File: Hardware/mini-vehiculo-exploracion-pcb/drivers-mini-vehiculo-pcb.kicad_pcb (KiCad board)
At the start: 2 copper layers, 7 parts, among them IC1 MAX8891EXK33_V+T, U1 TPS561208DDCR, U3 DRV8873HPWPRQ1, U4 DRV8873HPWPRQ1

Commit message: updated driver pcb
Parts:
- added C1: 0.1u, capacitores_driver:CAPC2012X88N, F.Cu at (75.1, 114.4)
- added C11: 1u, capacitores_driver:CAPC2012X88N, F.Cu at (61.0, 128.0)
- added C12: 0.1u, capacitores_driver:CAPC2012X88N, F.Cu at (75.1, 129.5)
- added C13: 47n, capacitores_driver:CAPC2012X140N, F.Cu at (61.6, 123.0)
- added C2: 0.1u, capacitores_driver:CAPC2012X88N, F.Cu at (75.1, 117.4)
- added C3: 1u, capacitores_driver:CAPC2012X88N, F.Cu at (75.1, 120.5)
- added C4: 1u, capacitores_driver:CAPC2012X88N, F.Cu at (75.1, 123.5)
- added C6: 1u, capacitores_driver:CAPC2012X88N, F.Cu at (66.6, 109.5)
- added C7: 0.1u, capacitores_driver:CAPC2012X88N, F.Cu at (75.1, 126.5)
- added C8: 47n, capacitores_driver:CAPC2012X140N, F.Cu at (58.6, 105.5)

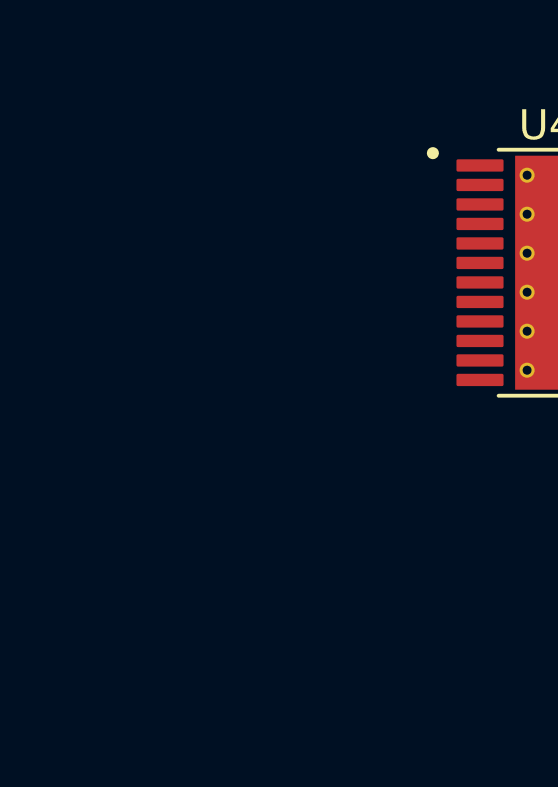
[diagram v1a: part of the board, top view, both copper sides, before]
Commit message: updated resistor footprint
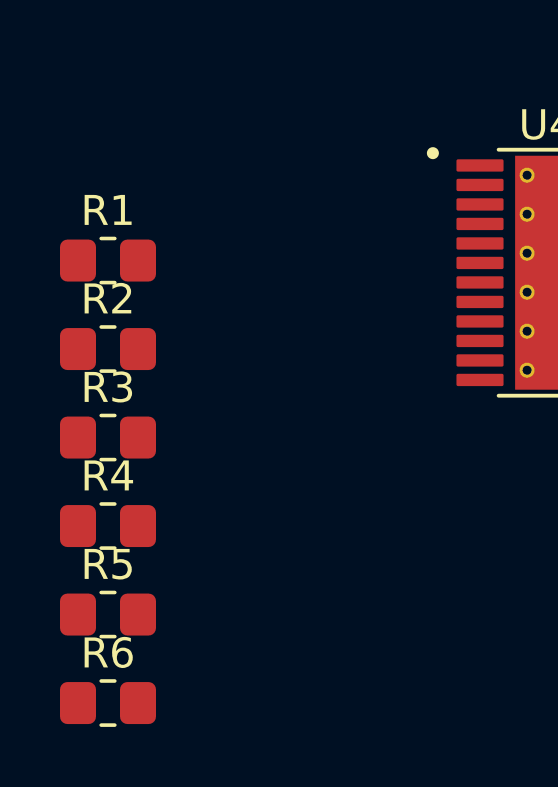
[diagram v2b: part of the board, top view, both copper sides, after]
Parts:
- added R1: 820, Resistor_SMD:R_0805_2012Metric_Pad1.20x1.40mm_HandSolder, F.Cu at (33.0, 124.2)
- added R2: 820, Resistor_SMD:R_0805_2012Metric_Pad1.20x1.40mm_HandSolder, F.Cu at (33.0, 127.2)
- added R3: 820, Resistor_SMD:R_0805_2012Metric_Pad1.20x1.40mm_HandSolder, F.Cu at (33.0, 130.2)
- added R4: 820, Resistor_SMD:R_0805_2012Metric_Pad1.20x1.40mm_HandSolder, F.Cu at (33.0, 133.1)
- added R5: 10k, Resistor_SMD:R_0805_2012Metric_Pad1.20x1.40mm_HandSolder, F.Cu at (33.0, 136.1)
- added R6: 10k, Resistor_SMD:R_0805_2012Metric_Pad1.20x1.40mm_HandSolder, F.Cu at (33.0, 139.0)

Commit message: updated pcb drv
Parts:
- added C1: 180u, EMZR160ARA221MF61G:CAPAE660X610N, F.Cu at (38.4, 61.5)
- added C7: 180u, EMZR160ARA221MF61G:CAPAE660X610N, F.Cu at (38.4, 109.5)
- added J1: Conn_01x08_Pin_drv, JST_Connectors:JST_8PIN, F.Cu at (54.0, 44.5)
- F1: value SMD200F_24-2920-2 -> SF-1206SA1500R-2; footprint SMD200F_24-2920:SMD200F2429202 -> SF-1206SA1500R-2:SF1206SA1500R2
- moved R2 64.4 mm to (39.5, 72.0)
- moved C4 50.0 mm to (72.6, 76.5)
- moved R1 48.7 mm to (35.0, 78.5)
- moved R5 47.1 mm to (40.5, 92.5)
- moved R3 46.9 mm to (41.0, 78.0)
- moved C2 42.3 mm to (66.6, 73.0)
- moved C11 39.1 mm to (112.5, 112.0)
- moved C5 39.1 mm to (112.5, 109.0)
- moved C10 35.8 mm to (67.4, 94.5)
- moved R6 34.8 mm to (37.0, 98.5)
- moved R4 34.5 mm to (42.5, 97.0)
- moved C12 29.4 mm to (62.0, 93.6), turned to 90 degrees
- moved C3 28.7 mm to (68.2, 80.8)
- moved C6 28.7 mm to (60.2, 76.8)
- moved C9 28.7 mm to (62.5, 99.3)
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- renumbered C12 to C10, C4 to C11, C13 to C12, C1 to C2, C6 to C3, C7 to C4, C3 to C5, C8 to C6, C2 to C8, C11 to C9, R2 to R1, R5 to R2, R1 to R3, R3 to R4, R6 to R5, R4 to R6, U3 to U1, U4 to U2, U1 to U3

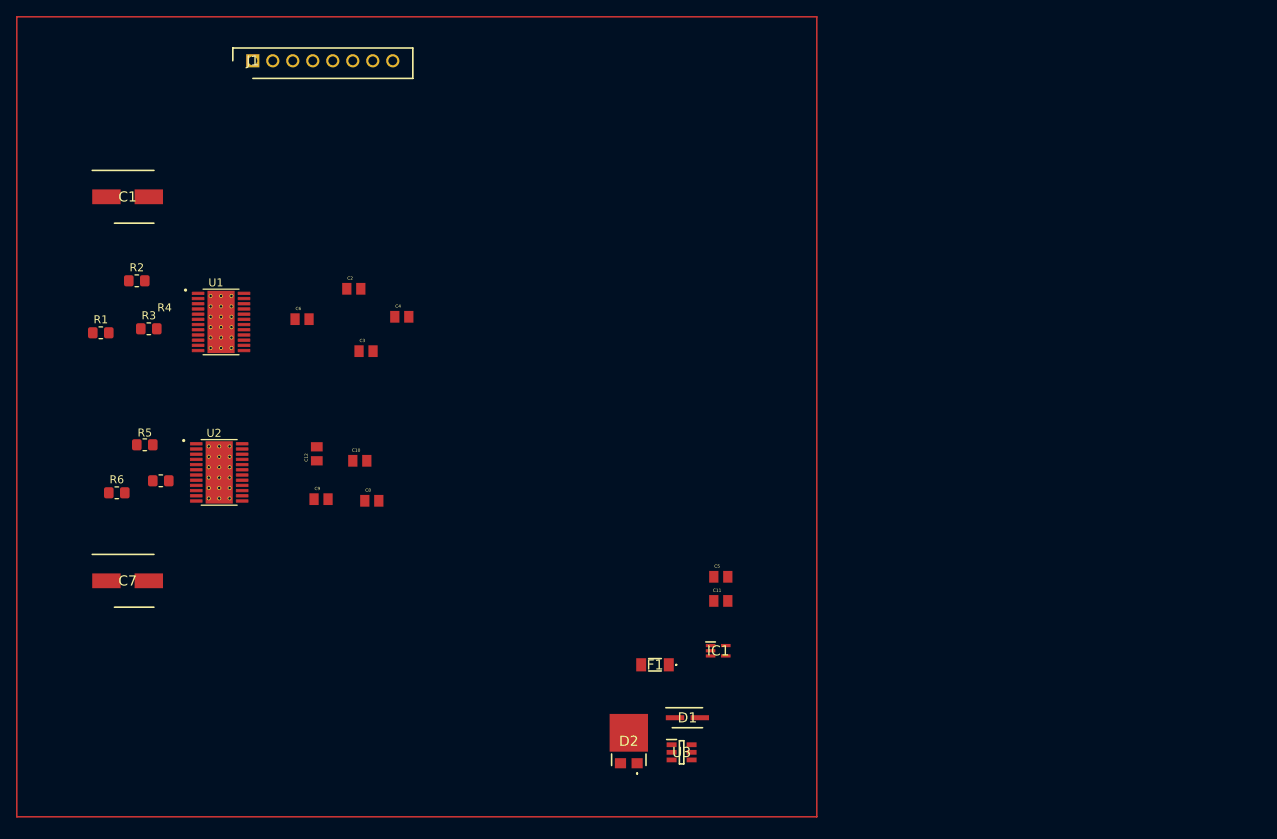
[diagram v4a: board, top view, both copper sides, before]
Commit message: Add netclassses, mounting holes and terminal block
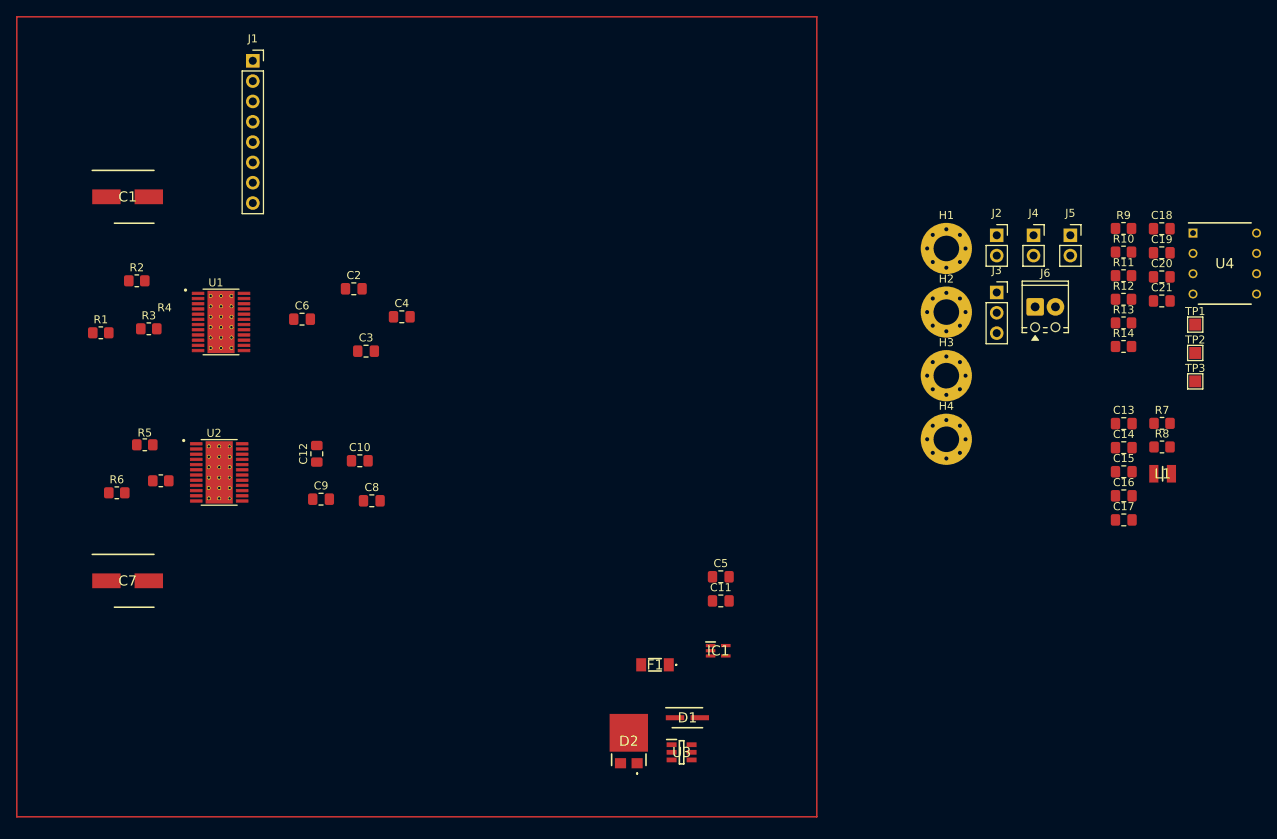
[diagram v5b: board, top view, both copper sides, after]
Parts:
- added C13: 10u, Capacitor_SMD:C_0805_2012Metric_Pad1.18x1.45mm_HandSolder, F.Cu at (162.9, 89.8)
- added C14: 100n, Capacitor_SMD:C_0805_2012Metric_Pad1.18x1.45mm_HandSolder, F.Cu at (162.9, 92.9)
- added C15: 47u, Capacitor_SMD:C_0805_2012Metric_Pad1.18x1.45mm_HandSolder, F.Cu at (162.9, 95.9)
- added C16: 1u, Capacitor_SMD:C_0805_2012Metric_Pad1.18x1.45mm_HandSolder, F.Cu at (162.9, 98.9)
- added C17: 1u, Capacitor_SMD:C_0805_2012Metric_Pad1.18x1.45mm_HandSolder, F.Cu at (162.9, 101.9)
- added C18: 10uF, Capacitor_SMD:C_0805_2012Metric_Pad1.18x1.45mm_HandSolder, F.Cu at (167.6, 65.5)
- added C19: 200nF, Capacitor_SMD:C_0805_2012Metric_Pad1.18x1.45mm_HandSolder, F.Cu at (167.6, 68.5)
- added C20: 10uF, Capacitor_SMD:C_0805_2012Metric_Pad1.18x1.45mm_HandSolder, F.Cu at (167.6, 71.5)
- added C21: 4.7u, Capacitor_SMD:C_0805_2012Metric_Pad1.18x1.45mm_HandSolder, F.Cu at (167.6, 74.5)
- added H1: MountingHole_Pad, MountingHole:MountingHole_3.2mm_M3_Pad_Via, F.Cu at (140.7, 68.0)
- added H2: MountingHole_Pad, MountingHole:MountingHole_3.2mm_M3_Pad_Via, F.Cu at (140.7, 75.9)
- added H3: MountingHole_Pad, MountingHole:MountingHole_3.2mm_M3_Pad_Via, F.Cu at (140.7, 83.9)
- added H4: MountingHole_Pad, MountingHole:MountingHole_3.2mm_M3_Pad_Via, F.Cu at (140.7, 91.8)
- added J2: Conn_01x02_Pin_drv, Connector_PinSocket_2.54mm:PinSocket_1x02_P2.54mm_Vertical, F.Cu at (147.0, 66.3)
- added J3: Conn_01x03_Pin, Connector_PinSocket_2.54mm:PinSocket_1x03_P2.54mm_Vertical, F.Cu at (147.0, 73.5)
- added J4: Conn_01x02_Motor1, Connector_PinSocket_2.54mm:PinSocket_1x02_P2.54mm_Vertical, F.Cu at (151.6, 66.3)
- added J5: Conn_01x02_Motor2, Connector_PinSocket_2.54mm:PinSocket_1x02_P2.54mm_Vertical, F.Cu at (156.2, 66.3)
- added J6: Battery_Terminal_01x02, TerminalBlock_Phoenix:TerminalBlock_Phoenix_MPT-0,5-2-2.54_1x02_P2.54mm_Horizontal, F.Cu at (151.8, 75.3)
- added L1: 4,7u, MLP2520S4R7MT0S1:INDC2520X100N, F.Cu at (167.7, 96.1)
- added R10: 10k, Resistor_SMD:R_0805_2012Metric_Pad1.20x1.40mm_HandSolder, F.Cu at (162.8, 68.4)
- added R11: 18k, Resistor_SMD:R_0805_2012Metric_Pad1.20x1.40mm_HandSolder, F.Cu at (162.8, 71.4)
- added R12: 20k, Resistor_SMD:R_0805_2012Metric_Pad1.20x1.40mm_HandSolder, F.Cu at (162.8, 74.3)
- added R13: 2k, Resistor_SMD:R_0805_2012Metric_Pad1.20x1.40mm_HandSolder, F.Cu at (162.8, 77.3)
- added R14: 2.7k, Resistor_SMD:R_0805_2012Metric_Pad1.20x1.40mm_HandSolder, F.Cu at (162.8, 80.2)
- added R7: 56,2k, Resistor_SMD:R_0805_2012Metric_Pad1.20x1.40mm_HandSolder, F.Cu at (167.7, 89.8)
- added R8: 10k, Resistor_SMD:R_0805_2012Metric_Pad1.20x1.40mm_HandSolder, F.Cu at (167.7, 92.8)
- added R9: 65k, Resistor_SMD:R_0805_2012Metric_Pad1.20x1.40mm_HandSolder, F.Cu at (162.8, 65.5)
- added TP1: Bat_div, TestPoint:TestPoint_Pad_1.5x1.5mm, F.Cu at (171.8, 77.5)
- added TP2: OP1_Out, TestPoint:TestPoint_Pad_1.5x1.5mm, F.Cu at (171.8, 81.0)
- added TP3: OP2_Out, TestPoint:TestPoint_Pad_1.5x1.5mm, F.Cu at (171.8, 84.6)
- added U4: LM358, LM358AN_NOPB:DIP794W53P254L959H508Q8N, F.Cu at (175.5, 69.8)
- C10, C11, C2, C3, C4, C5, C8, C9: footprint capacitores_driver:CAPC2012X88N -> Capacitor_SMD:C_0805_2012Metric_Pad1.18x1.45mm_HandSolder
- C12, C6: footprint capacitores_driver:CAPC2012X140N -> Capacitor_SMD:C_0805_2012Metric_Pad1.18x1.45mm_HandSolder
- J1: footprint JST_Connectors:JST_8PIN -> Connector_PinSocket_2.54mm:PinSocket_1x08_P2.54mm_Vertical
- U1, U2: footprint DRV8873HPWPRQ1:DRV8873HPWPRQ1 -> DRV8873HPWPRQ1:SOP65P640X120-25N
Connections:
- net Net-(U1-CPH) renamed /CPH1
- net Net-(U1-CPL) renamed /CPL1
- net Net-(U1-IPROPI1) renamed /IPROPI1_1
- net Net-(U1-IPROPI2) renamed /IPROPI2_1
- net Net-(U1-VCP) renamed /VCP1
- net Net-(U2-CPH) renamed /CPH2
- net Net-(U2-CPL) renamed /CPL2
- net Net-(U2-IPROPI1) renamed /IPROPI1_2
- net Net-(U2-IPROPI2) renamed /IPROPI2_2
- net Net-(U2-VCP) renamed /VCP2
- C11 pad 1: DVDD -> DVDD_2
- C5 pad 1: DVDD -> DVDD_1
- IC1 pad 2: Net-(IC1-GND) -> GND
- U1 pad 1: DVDD -> DVDD_1
- U1 pad 11: DVDD -> DVDD_1
- U1 pad 25: Net-(U1-EXP-Pad25) -> unconnected-(U1-EXP-Pad25)_18
- U1 pad 3: DVDD -> DVDD_1
- U1 pad P1: Net-(U1-EXP-Pad25) -> unconnected-(U1-EXP-Pad25)_5
- U1 pad P10: Net-(U1-EXP-Pad25) -> unconnected-(U1-EXP-Pad25)_15
- U1 pad P11: Net-(U1-EXP-Pad25) -> unconnected-(U1-EXP-Pad25)_8
- U1 pad P12: Net-(U1-EXP-Pad25) -> unconnected-(U1-EXP-Pad25)_4
- U1 pad P13: Net-(U1-EXP-Pad25) -> unconnected-(U1-EXP-Pad25)_9
- U1 pad P14: Net-(U1-EXP-Pad25) -> unconnected-(U1-EXP-Pad25)_16
- U1 pad P15: Net-(U1-EXP-Pad25) -> unconnected-(U1-EXP-Pad25)_6
- U1 pad P16: Net-(U1-EXP-Pad25) -> unconnected-(U1-EXP-Pad25)_10
- U1 pad P17: Net-(U1-EXP-Pad25) -> unconnected-(U1-EXP-Pad25)
- U1 pad P18: Net-(U1-EXP-Pad25) -> unconnected-(U1-EXP-Pad25)_11
- U1 pad P2: Net-(U1-EXP-Pad25) -> unconnected-(U1-EXP-Pad25)_1
- U1 pad P3: Net-(U1-EXP-Pad25) -> unconnected-(U1-EXP-Pad25)_14
- U1 pad P4: Net-(U1-EXP-Pad25) -> unconnected-(U1-EXP-Pad25)_7
- U1 pad P5: Net-(U1-EXP-Pad25) -> unconnected-(U1-EXP-Pad25)_2
- U1 pad P6: Net-(U1-EXP-Pad25) -> unconnected-(U1-EXP-Pad25)_3
- U1 pad P7: Net-(U1-EXP-Pad25) -> unconnected-(U1-EXP-Pad25)_13
- U1 pad P8: Net-(U1-EXP-Pad25) -> unconnected-(U1-EXP-Pad25)_17
- U1 pad P9: Net-(U1-EXP-Pad25) -> unconnected-(U1-EXP-Pad25)_12
- U2 pad 1: DVDD -> DVDD_2
- U2 pad 11: DVDD -> DVDD_2
- U2 pad 25: Net-(U2-EXP-Pad25) -> unconnected-(U2-EXP-Pad25)_7
- U2 pad 3: DVDD -> DVDD_2
- U2 pad P1: Net-(U2-EXP-Pad25) -> unconnected-(U2-EXP-Pad25)_12
- U2 pad P10: Net-(U2-EXP-Pad25) -> unconnected-(U2-EXP-Pad25)_11
- U2 pad P11: Net-(U2-EXP-Pad25) -> unconnected-(U2-EXP-Pad25)_8
- U2 pad P12: Net-(U2-EXP-Pad25) -> unconnected-(U2-EXP-Pad25)_1
- U2 pad P13: Net-(U2-EXP-Pad25) -> unconnected-(U2-EXP-Pad25)_15
- U2 pad P14: Net-(U2-EXP-Pad25) -> unconnected-(U2-EXP-Pad25)_3
- U2 pad P15: Net-(U2-EXP-Pad25) -> unconnected-(U2-EXP-Pad25)_14
- U2 pad P16: Net-(U2-EXP-Pad25) -> unconnected-(U2-EXP-Pad25)_17
- U2 pad P17: Net-(U2-EXP-Pad25) -> unconnected-(U2-EXP-Pad25)_13
- U2 pad P18: Net-(U2-EXP-Pad25) -> unconnected-(U2-EXP-Pad25)_6
- U2 pad P2: Net-(U2-EXP-Pad25) -> unconnected-(U2-EXP-Pad25)_2
- U2 pad P3: Net-(U2-EXP-Pad25) -> unconnected-(U2-EXP-Pad25)
- U2 pad P4: Net-(U2-EXP-Pad25) -> unconnected-(U2-EXP-Pad25)_18
- U2 pad P5: Net-(U2-EXP-Pad25) -> unconnected-(U2-EXP-Pad25)_5
- U2 pad P6: Net-(U2-EXP-Pad25) -> unconnected-(U2-EXP-Pad25)_16
- U2 pad P7: Net-(U2-EXP-Pad25) -> unconnected-(U2-EXP-Pad25)_10
- U2 pad P8: Net-(U2-EXP-Pad25) -> unconnected-(U2-EXP-Pad25)_9
- U2 pad P9: Net-(U2-EXP-Pad25) -> unconnected-(U2-EXP-Pad25)_4

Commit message: Revert "cambios"
This reverts commit 18d6c077649d06db3e4be51193d20dbced0bef3d, reversing
changes made to f53350afebab44693d0a4c4c217b64a1fc0c425b.
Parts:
- removed C13: 10u, Capacitor_SMD:C_0805_2012Metric_Pad1.18x1.45mm_HandSolder
- removed C14: 100n, Capacitor_SMD:C_0805_2012Metric_Pad1.18x1.45mm_HandSolder
- removed C15: 47u, Capacitor_SMD:C_0805_2012Metric_Pad1.18x1.45mm_HandSolder
- removed C16, C17: 1u, Capacitor_SMD:C_0805_2012Metric_Pad1.18x1.45mm_HandSolder
- removed C18, C20: 10uF, Capacitor_SMD:C_0805_2012Metric_Pad1.18x1.45mm_HandSolder
- removed C19: 200nF, Capacitor_SMD:C_0805_2012Metric_Pad1.18x1.45mm_HandSolder
- removed C21: 4.7u, Capacitor_SMD:C_0805_2012Metric_Pad1.18x1.45mm_HandSolder
- removed H1, H2, H3, H4: MountingHole_Pad, MountingHole:MountingHole_3.2mm_M3_Pad_Via
- removed J2: Conn_01x02_Pin_drv, Connector_PinSocket_2.54mm:PinSocket_1x02_P2.54mm_Vertical
- removed J3: Conn_01x03_Pin, Connector_PinSocket_2.54mm:PinSocket_1x03_P2.54mm_Vertical
- removed J4: Conn_01x02_Motor1, Connector_PinSocket_2.54mm:PinSocket_1x02_P2.54mm_Vertical
- removed J5: Conn_01x02_Motor2, Connector_PinSocket_2.54mm:PinSocket_1x02_P2.54mm_Vertical
- removed J6: Battery_Terminal_01x02, TerminalBlock_Phoenix:TerminalBlock_Phoenix_MPT-0,5-2-2.54_1x02_P2.54mm_Horizontal
- removed L1: 4,7u, MLP2520S4R7MT0S1:INDC2520X100N
- removed R10, R8: 10k, Resistor_SMD:R_0805_2012Metric_Pad1.20x1.40mm_HandSolder
- removed R11: 18k, Resistor_SMD:R_0805_2012Metric_Pad1.20x1.40mm_HandSolder
- removed R12: 20k, Resistor_SMD:R_0805_2012Metric_Pad1.20x1.40mm_HandSolder
- removed R13: 2k, Resistor_SMD:R_0805_2012Metric_Pad1.20x1.40mm_HandSolder
- removed R14: 2.7k, Resistor_SMD:R_0805_2012Metric_Pad1.20x1.40mm_HandSolder
- removed R7: 56,2k, Resistor_SMD:R_0805_2012Metric_Pad1.20x1.40mm_HandSolder
- removed R9: 65k, Resistor_SMD:R_0805_2012Metric_Pad1.20x1.40mm_HandSolder
- removed TP1: Bat_div, TestPoint:TestPoint_Pad_1.5x1.5mm
- removed TP2: OP1_Out, TestPoint:TestPoint_Pad_1.5x1.5mm
- removed TP3: OP2_Out, TestPoint:TestPoint_Pad_1.5x1.5mm
- removed U4: LM358, LM358AN_NOPB:DIP794W53P254L959H508Q8N
- C10, C11, C2, C3, C4, C5, C8, C9: footprint Capacitor_SMD:C_0805_2012Metric_Pad1.18x1.45mm_HandSolder -> capacitores_driver:CAPC2012X88N
- C12, C6: footprint Capacitor_SMD:C_0805_2012Metric_Pad1.18x1.45mm_HandSolder -> capacitores_driver:CAPC2012X140N
- J1: footprint Connector_PinSocket_2.54mm:PinSocket_1x08_P2.54mm_Vertical -> JST_Connectors:JST_8PIN
- U1, U2: footprint DRV8873HPWPRQ1:SOP65P640X120-25N -> DRV8873HPWPRQ1:DRV8873HPWPRQ1
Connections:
- net /CPH1 renamed Net-(U1-CPH)
- net /CPH2 renamed Net-(U2-CPH)
- net /CPL1 renamed Net-(U1-CPL)
- net /CPL2 renamed Net-(U2-CPL)
- net /IPROPI1_1 renamed Net-(U1-IPROPI1)
- net /IPROPI1_2 renamed Net-(U2-IPROPI1)
- net /IPROPI2_1 renamed Net-(U1-IPROPI2)
- net /IPROPI2_2 renamed Net-(U2-IPROPI2)
- net /VCP1 renamed Net-(U1-VCP)
- net /VCP2 renamed Net-(U2-VCP)
- C11 pad 1: DVDD_2 -> DVDD
- C5 pad 1: DVDD_1 -> DVDD
- IC1 pad 2: GND -> Net-(IC1-GND)
- U1 pad 1: DVDD_1 -> DVDD
- U1 pad 11: DVDD_1 -> DVDD
- U1 pad 25: unconnected-(U1-EXP-Pad25)_18 -> Net-(U1-EXP-Pad25)
- U1 pad 3: DVDD_1 -> DVDD
- U1 pad P1: unconnected-(U1-EXP-Pad25)_5 -> Net-(U1-EXP-Pad25)
- U1 pad P10: unconnected-(U1-EXP-Pad25)_15 -> Net-(U1-EXP-Pad25)
- U1 pad P11: unconnected-(U1-EXP-Pad25)_8 -> Net-(U1-EXP-Pad25)
- U1 pad P12: unconnected-(U1-EXP-Pad25)_4 -> Net-(U1-EXP-Pad25)
- U1 pad P13: unconnected-(U1-EXP-Pad25)_9 -> Net-(U1-EXP-Pad25)
- U1 pad P14: unconnected-(U1-EXP-Pad25)_16 -> Net-(U1-EXP-Pad25)
- U1 pad P15: unconnected-(U1-EXP-Pad25)_6 -> Net-(U1-EXP-Pad25)
- U1 pad P16: unconnected-(U1-EXP-Pad25)_10 -> Net-(U1-EXP-Pad25)
- U1 pad P17: unconnected-(U1-EXP-Pad25) -> Net-(U1-EXP-Pad25)
- U1 pad P18: unconnected-(U1-EXP-Pad25)_11 -> Net-(U1-EXP-Pad25)
- U1 pad P2: unconnected-(U1-EXP-Pad25)_1 -> Net-(U1-EXP-Pad25)
- U1 pad P3: unconnected-(U1-EXP-Pad25)_14 -> Net-(U1-EXP-Pad25)
- U1 pad P4: unconnected-(U1-EXP-Pad25)_7 -> Net-(U1-EXP-Pad25)
- U1 pad P5: unconnected-(U1-EXP-Pad25)_2 -> Net-(U1-EXP-Pad25)
- U1 pad P6: unconnected-(U1-EXP-Pad25)_3 -> Net-(U1-EXP-Pad25)
- U1 pad P7: unconnected-(U1-EXP-Pad25)_13 -> Net-(U1-EXP-Pad25)
- U1 pad P8: unconnected-(U1-EXP-Pad25)_17 -> Net-(U1-EXP-Pad25)
- U1 pad P9: unconnected-(U1-EXP-Pad25)_12 -> Net-(U1-EXP-Pad25)
- U2 pad 1: DVDD_2 -> DVDD
- U2 pad 11: DVDD_2 -> DVDD
- U2 pad 25: unconnected-(U2-EXP-Pad25)_7 -> Net-(U2-EXP-Pad25)
- U2 pad 3: DVDD_2 -> DVDD
- U2 pad P1: unconnected-(U2-EXP-Pad25)_12 -> Net-(U2-EXP-Pad25)
- U2 pad P10: unconnected-(U2-EXP-Pad25)_11 -> Net-(U2-EXP-Pad25)
- U2 pad P11: unconnected-(U2-EXP-Pad25)_8 -> Net-(U2-EXP-Pad25)
- U2 pad P12: unconnected-(U2-EXP-Pad25)_1 -> Net-(U2-EXP-Pad25)
- U2 pad P13: unconnected-(U2-EXP-Pad25)_15 -> Net-(U2-EXP-Pad25)
- U2 pad P14: unconnected-(U2-EXP-Pad25)_3 -> Net-(U2-EXP-Pad25)
- U2 pad P15: unconnected-(U2-EXP-Pad25)_14 -> Net-(U2-EXP-Pad25)
- U2 pad P16: unconnected-(U2-EXP-Pad25)_17 -> Net-(U2-EXP-Pad25)
- U2 pad P17: unconnected-(U2-EXP-Pad25)_13 -> Net-(U2-EXP-Pad25)
- U2 pad P18: unconnected-(U2-EXP-Pad25)_6 -> Net-(U2-EXP-Pad25)
- U2 pad P2: unconnected-(U2-EXP-Pad25)_2 -> Net-(U2-EXP-Pad25)
- U2 pad P3: unconnected-(U2-EXP-Pad25) -> Net-(U2-EXP-Pad25)
- U2 pad P4: unconnected-(U2-EXP-Pad25)_18 -> Net-(U2-EXP-Pad25)
- U2 pad P5: unconnected-(U2-EXP-Pad25)_5 -> Net-(U2-EXP-Pad25)
- U2 pad P6: unconnected-(U2-EXP-Pad25)_16 -> Net-(U2-EXP-Pad25)
- U2 pad P7: unconnected-(U2-EXP-Pad25)_10 -> Net-(U2-EXP-Pad25)
- U2 pad P8: unconnected-(U2-EXP-Pad25)_9 -> Net-(U2-EXP-Pad25)
- U2 pad P9: unconnected-(U2-EXP-Pad25)_4 -> Net-(U2-EXP-Pad25)
